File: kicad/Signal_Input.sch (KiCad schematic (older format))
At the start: 30 parts, among them J2 CONN_COAXIAL, J3 CONN_COAXIAL, J4 CONN_COAXIAL, T1 WBC16-1T, U10 MC12093, U12 TLV3501, U13 ADR5040, U9 LTC6957-3

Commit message: Reworked schematic and layout [to review]
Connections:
- net CHA_FILTA renamed EXTREF_FILTA
- net CHA_FILTB renamed EXTREF_FILTB
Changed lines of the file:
@@
 $Descr A4 11693 8268
 encoding utf-8
-Sheet 5 5
+Sheet 4 5
 Title "FrequnecyCounter"
 Date "2017-07-19"
@@
 $EndDescr
 $Comp
-L GND #PWR0102
+L GND #PWR045
 U 1 1 595E1304
 P 3725 1675
-F 0 "#PWR0102" H 3725 1425 50  0001 C CNN
+F 0 "#PWR045" H 3725 1425 50  0001 C CNN
 F 1 "GND" H 3725 1525 50  0000 C CNN
 F 2 "" H 3725 1675 50  0001 C CNN
@@
 $EndComp
 $Comp
-L GND #PWR0103
+L GND #PWR046
 U 1 1 595E15F9
 P 3175 1875
-F 0 "#PWR0103" H 3175 1625 50  0001 C CNN
+F 0 "#PWR046" H 3175 1625 50  0001 C CNN
 F 1 "GND" H 3175 1725 50  0000 C CNN
 F 2 "" H 3175 1875 50  0001 C CNN
@@
 $EndComp
 $Comp
-L GND #PWR0104
+L GND #PWR047
 U 1 1 595E4D57
 P 6325 2225
-F 0 "#PWR0104" H 6325 1975 50  0001 C CNN
+F 0 "#PWR047" H 6325 1975 50  0001 C CNN
 F 1 "GND" H 6325 2075 50  0000 C CNN
 F 2 "" H 6325 2225 50  0001 C CNN
@@
 $EndComp
 $Comp
-L GND #PWR0105
+L GND #PWR048
 U 1 1 595E55DF
 P 5975 3925
-F 0 "#PWR0105" H 5975 3675 50  0001 C CNN
+F 0 "#PWR048" H 5975 3675 50  0001 C CNN
 F 1 "GND" H 5975 3775 50  0000 C CNN
 F 2 "" H 5975 3925 50  0001 C CNN
@@
 $EndComp
 $Comp
-L +3.3V #PWR0106
+L +3.3V #PWR049
 U 1 1 595E5A7F
 P 4325 3075
-F 0 "#PWR0106" H 4325 2925 50  0001 C CNN
+F 0 "#PWR049" H 4325 2925 50  0001 C CNN
 F 1 "+3.3V" H 4325 3215 50  0000 C CNN
 F 2 "" H 4325 3075 50  0001 C CNN
@@
 $EndComp
 $Comp
-L GND #PWR0107
+L GND #PWR050
 U 1 1 595E5BA0
 P 4325 3425
-F 0 "#PWR0107" H 4325 3175 50  0001 C CNN
+F 0 "#PWR050" H 4325 3175 50  0001 C CNN
 F 1 "GND" H 4325 3275 50  0000 C CNN
 F 2 "" H 4325 3425 50  0001 C CNN
@@
 $EndComp
 $Comp
-L GND #PWR0108
+L GND #PWR051
 U 1 1 595E5D32
 P 4975 4300
-F 0 "#PWR0108" H 4975 4050 50  0001 C CNN
+F 0 "#PWR051" H 4975 4050 50  0001 C CNN
 F 1 "GND" H 4975 4150 50  0000 C CNN
 F 2 "" H 4975 4300 50  0001 C CNN
@@
 $EndComp
 $Comp
-L GND #PWR0109
+L GND #PWR052
 U 1 1 595E6248
 P 4750 4300
-F 0 "#PWR0109" H 4750 4050 50  0001 C CNN
+F 0 "#PWR052" H 4750 4050 50  0001 C CNN
 F 1 "GND" H 4750 4150 50  0000 C CNN
 F 2 "" H 4750 4300 50  0001 C CNN
@@
 $EndComp
 $Comp
-L GND #PWR0110
+L GND #PWR053
 U 1 1 595E6503
 P 3625 4275
-F 0 "#PWR0110" H 3625 4025 50  0001 C CNN
+F 0 "#PWR053" H 3625 4025 50  0001 C CNN
 F 1 "GND" H 3625 4125 50  0000 C CNN
 F 2 "" H 3625 4275 50  0001 C CNN
@@
 $EndComp
 $Comp
-L GND #PWR0111
+L GND #PWR054
 U 1 1 595E7846
 P 1575 3925
-F 0 "#PWR0111" H 1575 3675 50  0001 C CNN
+F 0 "#PWR054" H 1575 3675 50  0001 C CNN
 F 1 "GND" H 1575 3775 50  0000 C CNN
 F 2 "" H 1575 3925 50  0001 C CNN
@@
 Ext_Ref
 $Comp
-L GND #PWR0112
+L GND #PWR055
 U 1 1 595E865F
 P 1900 1875
-F 0 "#PWR0112" H 1900 1625 50  0001 C CNN
+F 0 "#PWR055" H 1900 1625 50  0001 C CNN
 F 1 "GND" H 1900 1725 50  0000 C CNN
 F 2 "" H 1900 1875 50  0001 C CNN
@@
 $EndComp
 $Comp
-L +3.3V #PWR0113
+L +3.3V #PWR056
 U 1 1 595E9F37
 P 6050 1875
-F 0 "#PWR0113" H 6050 1725 50  0001 C CNN
+F 0 "#PWR056" H 6050 1725 50  0001 C CNN
 F 1 "+3.3V" H 6050 2015 50  0000 C CNN
 F 2 "" H 6050 1875 50  0001 C CNN
@@
 Clk_A
 $Comp
-L +3.3V #PWR0114
+L +3.3V #PWR057
 U 1 1 595EC3C2
 P 6175 4075
-F 0 "#PWR0114" H 6175 3925 50  0001 C CNN
+F 0 "#PWR057" H 6175 3925 50  0001 C CNN
 F 1 "+3.3V" H 6175 4215 50  0000 C CNN
 F 2 "" H 6175 4075 50  0001 C CNN
@@
 $EndComp
 $Comp
-L GND #PWR0115
+L GND #PWR058
 U 1 1 59655519
 P 6050 2225
-F 0 "#PWR0115" H 6050 1975 50  0001 C CNN
+F 0 "#PWR058" H 6050 1975 50  0001 C CNN
 F 1 "GND" H 6050 2075 50  0000 C CNN
 F 2 "" H 6050 2225 50  0001 C CNN
@@
 $EndComp
 Text HLabel 6150 875  2    60   Input ~ 0
-CHA_FILTA
+EXTREF_FILTA
 Text HLabel 5950 875  0    60   Input ~ 0
-CHA_FILTB
-$Comp
-L GND #PWR0116
+EXTREF_FILTB
+$Comp
+L GND #PWR059
 U 1 1 59659874
 P 8050 2075
-F 0 "#PWR0116" H 8050 1825 50  0001 C CNN
+F 0 "#PWR059" H 8050 1825 50  0001 C CNN
 F 1 "GND" H 8050 1925 50  0000 C CNN
 F 2 "" H 8050 2075 50  0001 C CNN
@@
 IN-
 $Comp
-L GND #PWR0117
+L GND #PWR060
 U 1 1 596CACB7
 P 7175 2500
-F 0 "#PWR0117" H 7175 2250 50  0001 C CNN
+F 0 "#PWR060" H 7175 2250 50  0001 C CNN
 F 1 "GND" H 7175 2350 50  0000 C CNN
 F 2 "" H 7175 2500 50  0001 C CNN
@@
 Connection ~ 5975 3900
 $Comp
-L GND #PWR0118
+L GND #PWR061
 U 1 1 59C3FC42
 P 2400 4175
-F 0 "#PWR0118" H 2400 3925 50  0001 C CNN
+F 0 "#PWR061" H 2400 3925 50  0001 C CNN
 F 1 "GND" H 2400 4025 50  0000 C CNN
 F 2 "" H 2400 4175 50  0001 C CNN
@@
 Connection ~ 7275 3550
 $Comp
-L GND #PWR0119
+L GND #PWR062
 U 1 1 59DBEE23
-P 7275 3925
-F 0 "#PWR0119" H 7275 3675 50  0001 C CNN
-F 1 "GND" H 7275 3775 50  0000 C CNN
-F 2 "" H 7275 3925 50  0001 C CNN
-F 3 "" H 7275 3925 50  0001 C CNN
-	1    7275 3925
-	1    0    0    -1
-$EndComp
-$Comp
-L +1.2V #PWR0120
+P 7275 3950
+F 0 "#PWR062" H 7275 3700 50  0001 C CNN
+F 1 "GND" H 7275 3800 50  0000 C CNN
+F 2 "" H 7275 3950 50  0001 C CNN
+F 3 "" H 7275 3950 50  0001 C CNN
+	1    7275 3950
+	1    0    0    -1
+$EndComp
+$Comp
+L +1.2V #PWR063
 U 1 1 59DBFDA3
-P 7275 3175
-F 0 "#PWR0120" H 7275 3315 20  0001 C CNN
-F 1 "+1.2V" H 7275 3285 30  0000 C CNN
-F 2 "" H 7275 3175 60  0000 C CNN
-F 3 "" H 7275 3175 60  0000 C CNN
-	1    7275 3175
+P 7275 3150
+F 0 "#PWR063" H 7275 3290 20  0001 C CNN
+F 1 "+1.2V" H 7275 3260 30  0000 C CNN
+F 2 "" H 7275 3150 60  0000 C CNN
+F 3 "" H 7275 3150 60  0000 C CNN
+	1    7275 3150
 	1    0    0    -1
 $EndComp
@@
 $EndComp
 $Comp
-L GND #PWR0121
+L GND #PWR064
 U 1 1 59DC2142
-P 1575 5650
-F 0 "#PWR0121" H 1575 5400 50  0001 C CNN
-F 1 "GND" H 1575 5500 50  0000 C CNN
-F 2 "" H 1575 5650 50  0001 C CNN
-F 3 "" H 1575 5650 50  0001 C CNN
-	1    1575 5650
+P 1575 5675
+F 0 "#PWR064" H 1575 5425 50  0001 C CNN
+F 1 "GND" H 1575 5525 50  0000 C CNN
+F 2 "" H 1575 5675 50  0001 C CNN
+F 3 "" H 1575 5675 50  0001 C CNN
+	1    1575 5675
 	1    0    0    -1
 $EndComp
@@
 $EndComp
 $Comp
-L +3.3V #PWR0122
+L +3.3V #PWR065
 U 1 1 59DC38DE
 P 4900 5975
-F 0 "#PWR0122" H 4900 5825 50  0001 C CNN
+F 0 "#PWR065" H 4900 5825 50  0001 C CNN
 F 1 "+3.3V" H 4900 6115 50  0000 C CNN
 F 2 "" H 4900 5975 50  0001 C CNN
@@
 Connection ~ 5200 6350
 $Comp
-L GND #PWR0123
+L GND #PWR066
 U 1 1 59DC418D
 P 5200 7075
-F 0 "#PWR0123" H 5200 6825 50  0001 C CNN
+F 0 "#PWR066" H 5200 6825 50  0001 C CNN
 F 1 "GND" H 5200 6925 50  0000 C CNN
 F 2 "" H 5200 7075 50  0001 C CNN
@@
 $EndComp
 $Comp
-L GND #PWR0124
+L GND #PWR067
 U 1 1 59DC41EF
 P 5425 6550
-F 0 "#PWR0124" H 5425 6300 50  0001 C CNN
+F 0 "#PWR067" H 5425 6300 50  0001 C CNN
 F 1 "GND" H 5425 6400 50  0000 C CNN
 F 2 "" H 5425 6550 50  0001 C CNN
@@
 $EndComp
 $Comp
-L +3.3V #PWR0125
+L +3.3V #PWR068
 U 1 1 59DC70AC
 P 3800 5200
-F 0 "#PWR0125" H 3800 5050 50  0001 C CNN
+F 0 "#PWR068" H 3800 5050 50  0001 C CNN
 F 1 "+3.3V" H 3800 5340 50  0000 C CNN
 F 2 "" H 3800 5200 50  0001 C CNN
@@
 $EndComp
 $Comp
-L GND #PWR0126
+L GND #PWR069
 U 1 1 59DC70FA
 P 3800 6000
-F 0 "#PWR0126" H 3800 5750 50  0001 C CNN
+F 0 "#PWR069" H 3800 5750 50  0001 C CNN
 F 1 "GND" H 3800 5850 50  0000 C CNN
 F 2 "" H 3800 6000 50  0001 C CNN
@@
 $EndComp
 $Comp
-L GND #PWR0127
+L GND #PWR070
 U 1 1 59DD57B6
 P 2375 5900
-F 0 "#PWR0127" H 2375 5650 50  0001 C CNN
+F 0 "#PWR070" H 2375 5650 50  0001 C CNN
 F 1 "GND" H 2375 5750 50  0000 C CNN
 F 2 "" H 2375 5900 50  0001 C CNN
@@
 	4900 5975 5200 5975
 $Comp
-L GND #PWR0128
+L GND #PWR071
 U 1 1 59DE4F7D
 P 4900 6275
-F 0 "#PWR0128" H 4900 6025 50  0001 C CNN
+F 0 "#PWR071" H 4900 6025 50  0001 C CNN
 F 1 "GND" H 4900 6125 50  0000 C CNN
 F 2 "" H 4900 6275 50  0001 C CNN
@@
 	1    0    0    -1
 $EndComp
+Wire Wire Line
+	7275 3950 7275 3925
+Wire Wire Line
+	7275 3150 7275 3175
+Wire Wire Line
+	1575 5675 1575 5650
 $EndSCHEMATC

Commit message: some small schematic and layout changes [completed]
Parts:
- removed C50: 100n, Capacitors_SMD:C_0603_HandSoldering, symbol C
- removed D4: BAV99, TO_SOT_Packages_SMD:SOT-23, symbol BAV99
- removed R23, R36: 1k, Resistors_SMD:R_0603_HandSoldering, symbol R
- removed R35: 100k, Resistors_SMD:R_0603_HandSoldering, symbol R
- removed U13: ADR5040, TO_SOT_Packages_SMD:SOT-323_SC-70_Handsoldering, symbol ADR5040
- added R18, R19: 100R, Resistors_SMD:R_0603_HandSoldering, symbol R
- added V2: HSMS-281C-TR1G, TO_SOT_Packages_SMD:SOT-323_SC-70_Handsoldering, symbol HSMS-281C-TR1G
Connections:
- net CH_A: now also R18.1; no longer J3.1 (In)
- net CH_B: now also R19.1, V2.1, V2.2; no longer J4.1 (In)
- net GND: now also U12.2 (IN-), U12.8 (SHDN), V2.3
- new net: J3.1 (In), R18.2
- new net: J4.1 (In), R19.2
- no-connect marks 3 -> 1
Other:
- note added: "fg = 2.3405MHz\n"
- note added: "fg = 3.183MHz\n"
- moved on the sheet: C43, C44, C45, C46, C47, C48, C49, C51, D3, J2, R17, R22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

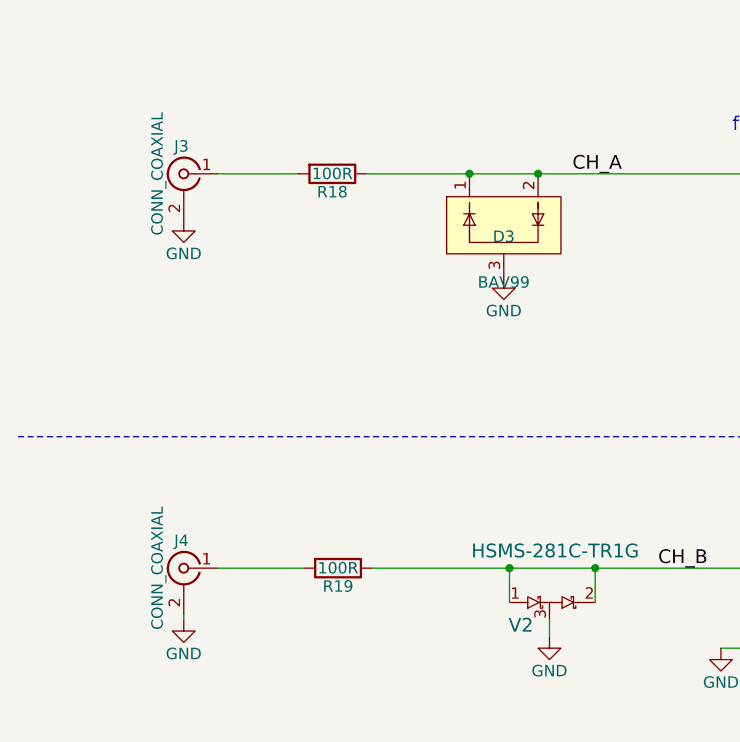
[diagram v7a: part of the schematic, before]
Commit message: Small layout and schematic changes
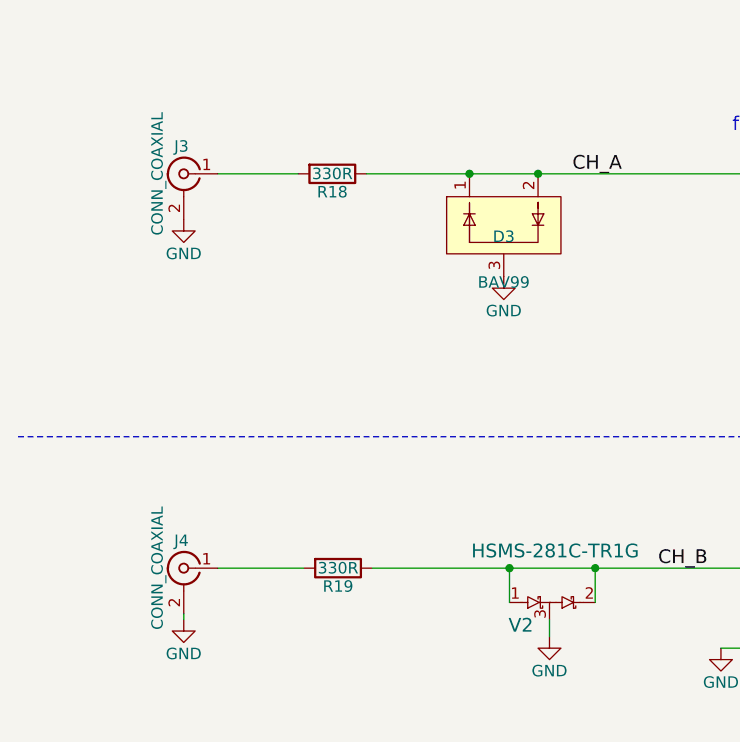
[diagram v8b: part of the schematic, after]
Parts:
- R18, R19: value 100R -> 330R
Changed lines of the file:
@@
 EESchema Schematic File Version 2
+LIBS:FrequnecyCounter-rescue
 LIBS:power
 LIBS:device
@@
 P 2250 5450
 F 0 "R19" V 2330 5450 50  0000 C CNN
-F 1 "100R" V 2250 5450 50  0000 C CNN
+F 1 "330R" V 2250 5450 50  0000 C CNN
 F 2 "Resistors_SMD:R_0603_HandSoldering" V 2180 5450 50  0001 C CNN
 F 3 "" H 2250 5450 50  0001 C CNN
@@
 P 2225 3725
 F 0 "R18" V 2305 3725 50  0000 C CNN
-F 1 "100R" V 2225 3725 50  0000 C CNN
+F 1 "330R" V 2225 3725 50  0000 C CNN
 F 2 "Resistors_SMD:R_0603_HandSoldering" V 2155 3725 50  0001 C CNN
 F 3 "" H 2225 3725 50  0001 C CNN
